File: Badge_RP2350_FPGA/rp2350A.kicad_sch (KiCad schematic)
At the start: 33 parts, among them J4 SM03B-SRSS-TB, SW1 SW_Push, SW2 SW_Push, U1 RP2350_60QFN, U3 W25Q128JVS, Y1 ABM8-272-T3

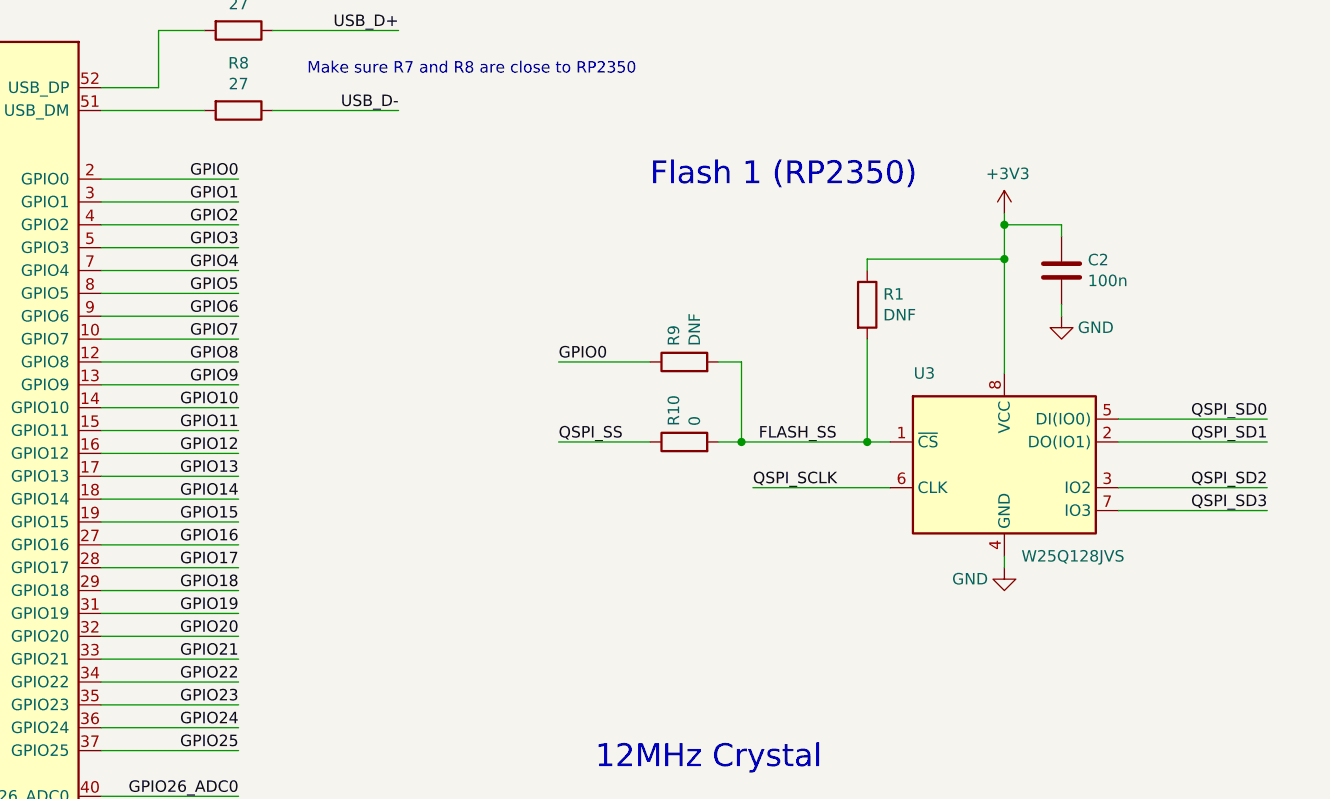
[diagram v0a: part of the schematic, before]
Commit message: add jtag connection
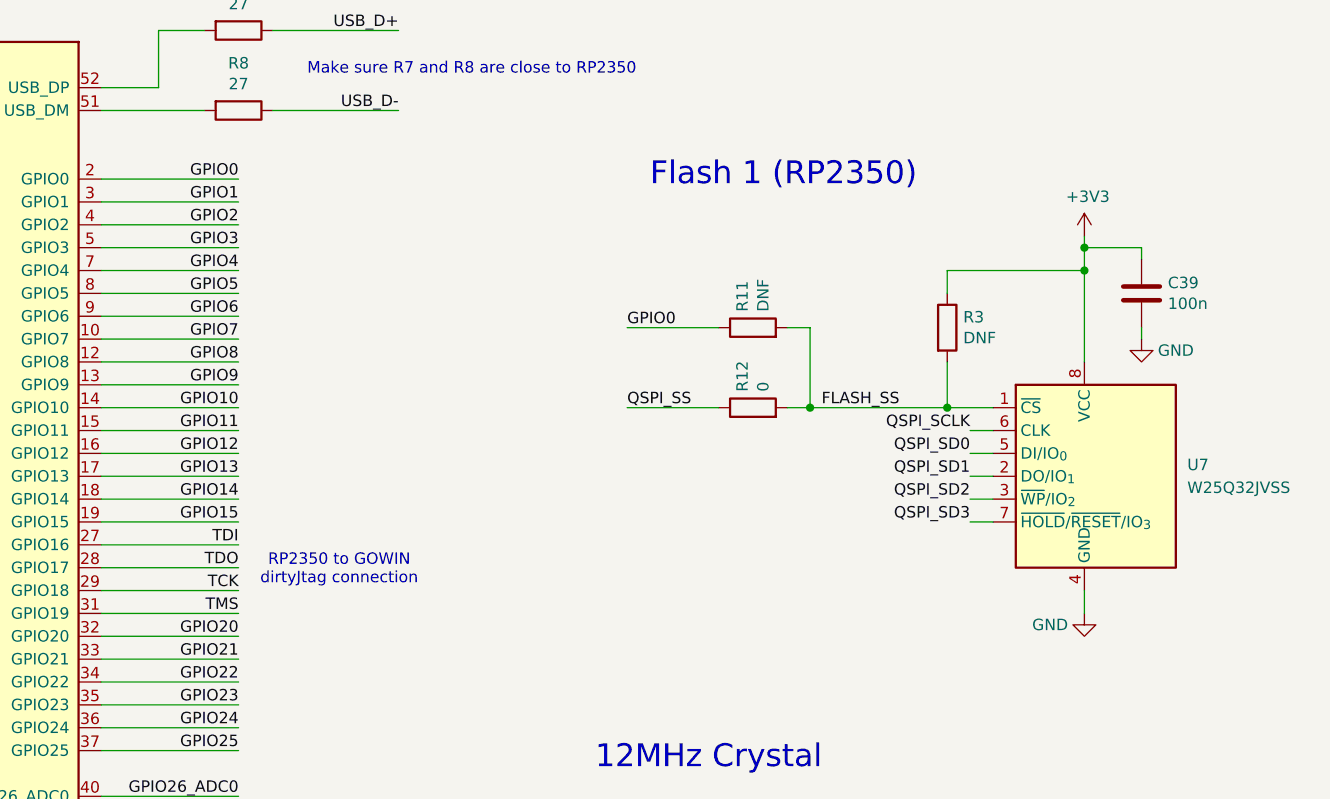
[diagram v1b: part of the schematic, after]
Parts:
- removed C2: 100n, Capacitor_SMD:C_0402_1005Metric, symbol Device:C
- removed R1, R9: DNF, Resistor_SMD:R_0402_1005Metric, symbol Device:R
- removed R10: 0, Resistor_SMD:R_0402_1005Metric, symbol Device:R
- removed U3: W25Q128JVS, Package_SO:SOIC-8_5.23x5.23mm_P1.27mm, symbol Memory_Flash:W25Q128JVS
- added C39: 100n, Capacitor_SMD:C_0402_1005Metric, symbol Device:C
- added R11, R3: DNF, Resistor_SMD:R_0402_1005Metric, symbol Device:R
- added R12: 0, Resistor_SMD:R_0402_1005Metric, symbol Device:R
- added U7: W25Q32JVSS, Package_SO:SOIC-8_5.3x5.3mm_P1.27mm, symbol Memory_Flash:W25Q32JVSS
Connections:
- net +3V3: now also C39.1, R3.1, U7.8 (VCC)
- net FLASH_SS: now also R11.2, R12.2, R3.2, U7.1 (~{CS})
- net GND: now also C39.2, U7.4 (GND)
- net GPIO0: now also R11.1
- net QSPI_SCLK: now also U7.6 (CLK)
- net QSPI_SD0: now also U7.5 (DI/IO_{0})
- net QSPI_SD1: now also U7.2 (DO/IO_{1})
- net QSPI_SD2: now also U7.3 (~{WP}/IO_{2})
- net QSPI_SD3: now also U7.7 (~{HOLD}/~{RESET}/IO_{3})
- net QSPI_SS: now also R12.1
- net GPIO16 renamed TDI
- net GPIO17 renamed TDO
- net GPIO18 renamed TCK
- net GPIO19 renamed TMS
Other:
- note added: "RP2350 to GOWIN dirtyJtag connection"

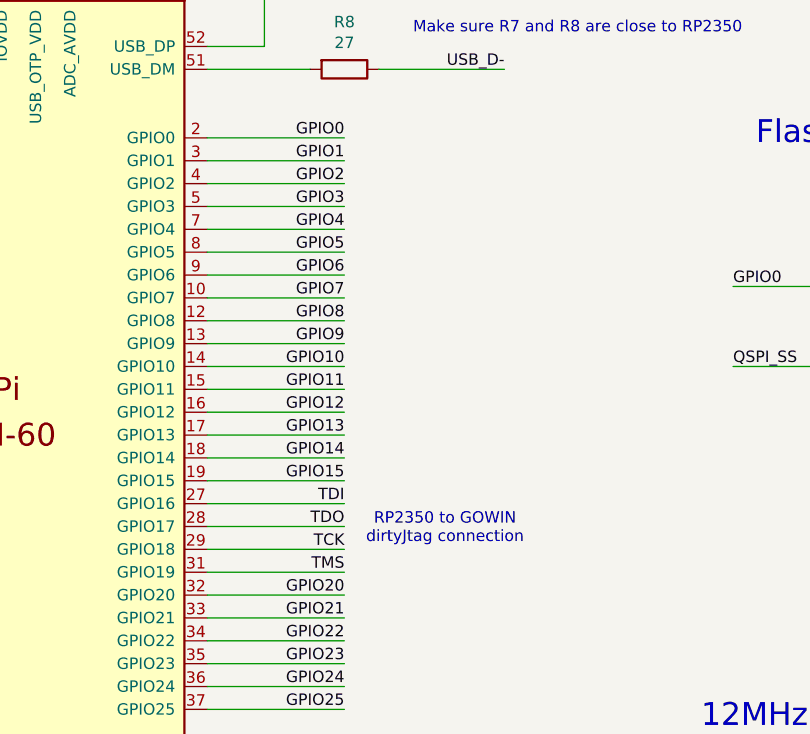
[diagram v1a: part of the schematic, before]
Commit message: add buttons by Arianna and make Flash 2 shared between 2 chips
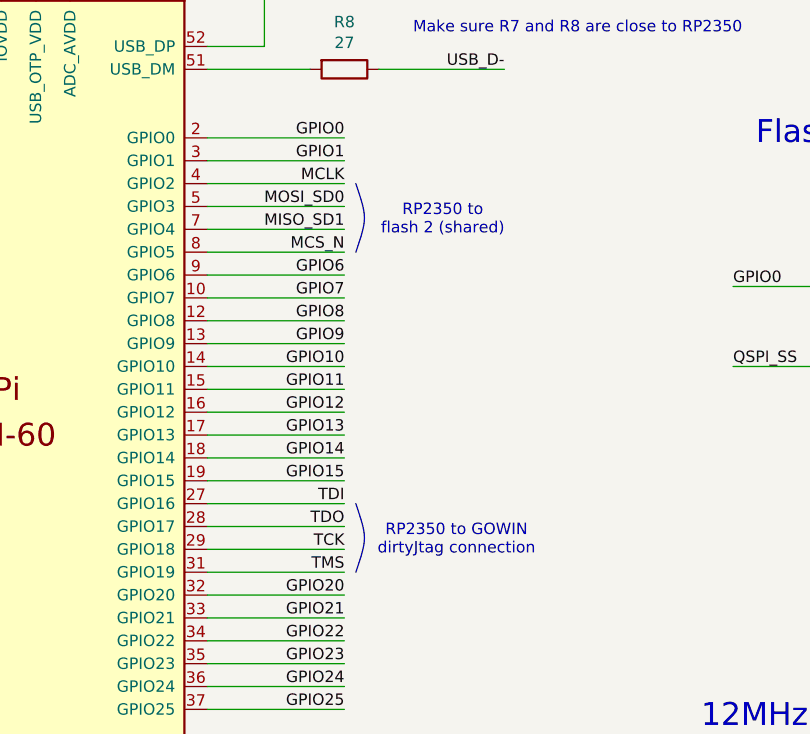
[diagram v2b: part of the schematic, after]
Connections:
- net GPIO2 renamed MCLK
- net GPIO3 renamed MOSI_SD0
- net GPIO4 renamed MISO_SD1
- net GPIO5 renamed MCS_N
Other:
- note added: "RP2350 to flash 2 (shared)"
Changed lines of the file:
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@@
 	(generator_version "10.0")
 	(paper "A4")
+	(bezier
+		(pts
+			(xy 156.21 76.2) (xy 157.48 80.01) (xy 157.48 80.01) (xy 156.21 83.82)
+		)
+		(stroke
+			(width 0)
+			(type default)
+		)
+		(fill
+			(type none)
+		)
+	)
+	(bezier
+		(pts
+			(xy 156.21 111.76) (xy 157.48 115.57) (xy 157.48 115.57) (xy 156.21 119.38)
+		)
+		(stroke
+			(width 0)
+			(type default)
+		)
+		(fill
+			(type none)
+		)
+	)
 	(circle
 		(center 43.18 65.405)
@@
 		)
 	)
+	(text "RP2350 to \nflash 2 (shared)"
+		(exclude_from_sim no)
+		(at 165.862 80.264 0)
+		(effects
+			(font
+				(size 1.27 1.27)
+			)
+		)
+	)
 	(text "JST Debug Connector"
 		(exclude_from_sim no)
@@
 	(text "RP2350 to GOWIN \ndirtyJtag connection"
 		(exclude_from_sim no)
-		(at 166.116 114.554 0)
+		(at 167.386 115.824 0)
 		(effects
 			(font
@@
 		)
 	)
-	(label "GPIO5"
-		(at 154.94 83.82 180)
-		(effects
-			(font
-				(size 1.27 1.27)
-			)
-			(justify right bottom)
-		)
-	)
 	(label "GPIO8"
 		(at 154.94 91.44 180)
@@
 		)
 	)
-	(label "GPIO2"
-		(at 154.94 76.2 180)
-		(effects
-			(font
-				(size 1.27 1.27)
-			)
-			(justify right bottom)
-		)
-	)
 	(label "GPIO27_ADC1"
 		(at 154.94 142.24 180)
@@
 		)
 	)
-	(label "GPIO4"
-		(at 154.94 81.28 180)
-		(effects
-			(font
-				(size 1.27 1.27)
-			)
-			(justify right bottom)
-		)
-	)
 	(label "QSPI_SD0"
 		(at 236.22 101.6 180)
@@
 		)
 	)
+	(label "MCS_N"
+		(at 154.94 83.82 180)
+		(effects
+			(font
+				(size 1.27 1.27)
+			)
+			(justify right bottom)
+		)
+	)
 	(label "QSPI_SCLK"
 		(at 236.22 99.06 180)
@@
 		)
 	)
+	(label "MCLK"
+		(at 154.94 76.2 180)
+		(effects
+			(font
+				(size 1.27 1.27)
+			)
+			(justify right bottom)
+		)
+	)
 	(label "USB_D-"
 		(at 172.72 63.5 180)
@@
 		)
 	)
-	(label "GPIO3"
-		(at 154.94 78.74 180)
-		(effects
-			(font
-				(size 1.27 1.27)
-			)
-			(justify right bottom)
-		)
-	)
 	(label "QSPI_SD3"
 		(at 236.22 109.22 180)
@@
 		)
 	)
+	(label "MOSI_SD0"
+		(at 154.94 78.74 180)
+		(effects
+			(font
+				(size 1.27 1.27)
+			)
+			(justify right bottom)
+		)
+	)
 	(label "GPIO12"
 		(at 154.94 101.6 180)
@@
 		)
 	)
+	(label "MISO_SD1"
+		(at 154.94 81.28 180)
+		(effects
+			(font
+				(size 1.27 1.27)
+			)
+			(justify right bottom)
+		)
+	)

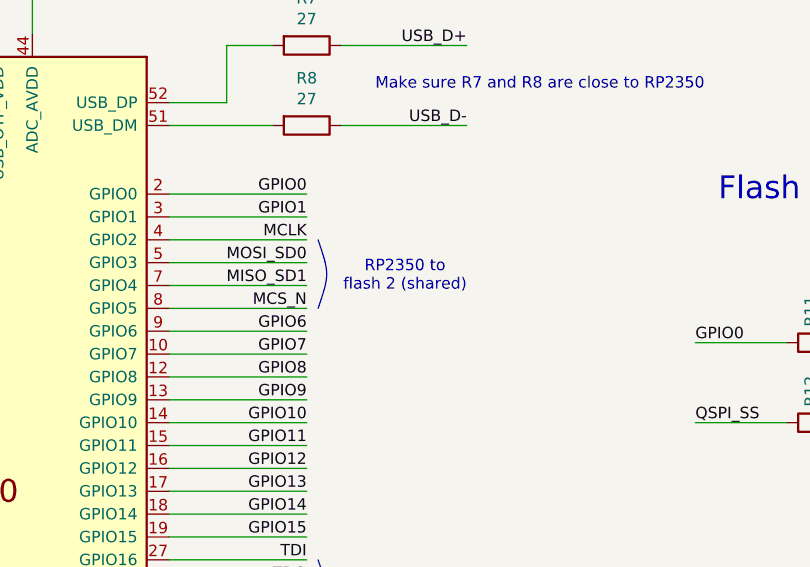
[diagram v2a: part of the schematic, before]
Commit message: delete Core directory - not the right repository
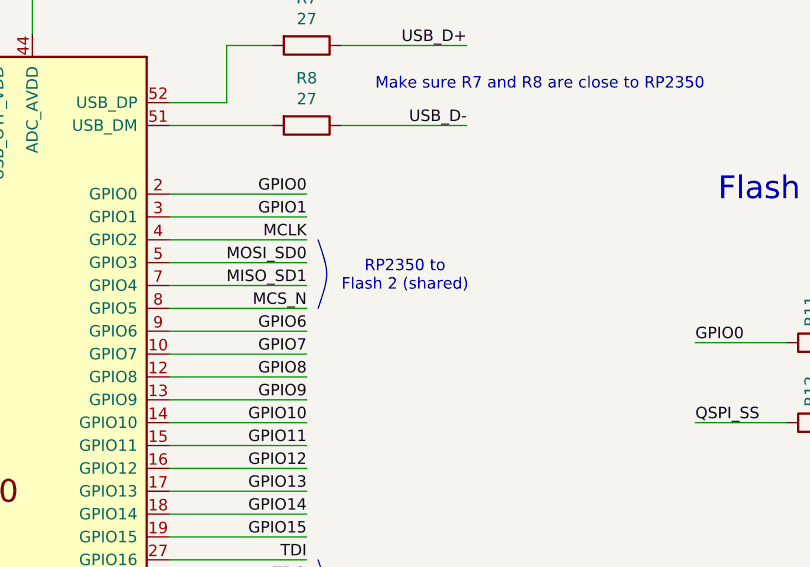
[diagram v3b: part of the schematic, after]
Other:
- note added: "RP2350 to Flash 2 (shared)"
- note removed: "RP2350 to flash 2 (shared)"
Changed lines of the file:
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@@
 		)
 	)
-	(text "RP2350 to \nflash 2 (shared)"
+	(text "RP2350 to \nFlash 2 (shared)"
 		(exclude_from_sim no)
 		(at 165.862 80.264 0)

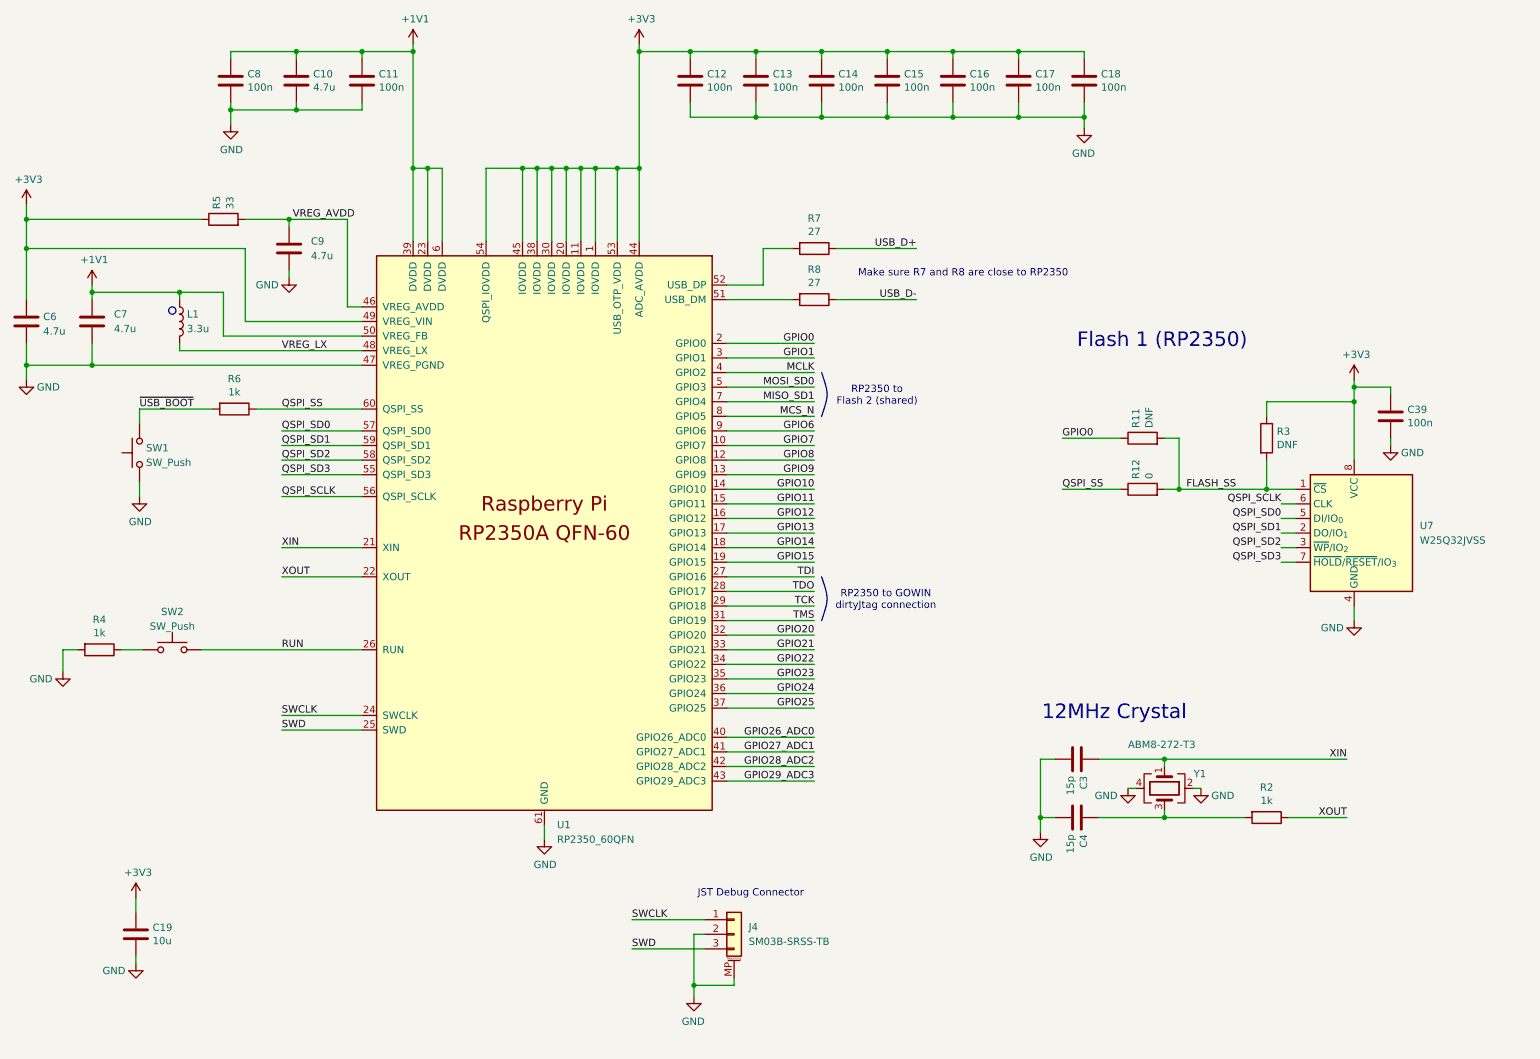
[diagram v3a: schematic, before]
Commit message: add type c port and uart connections
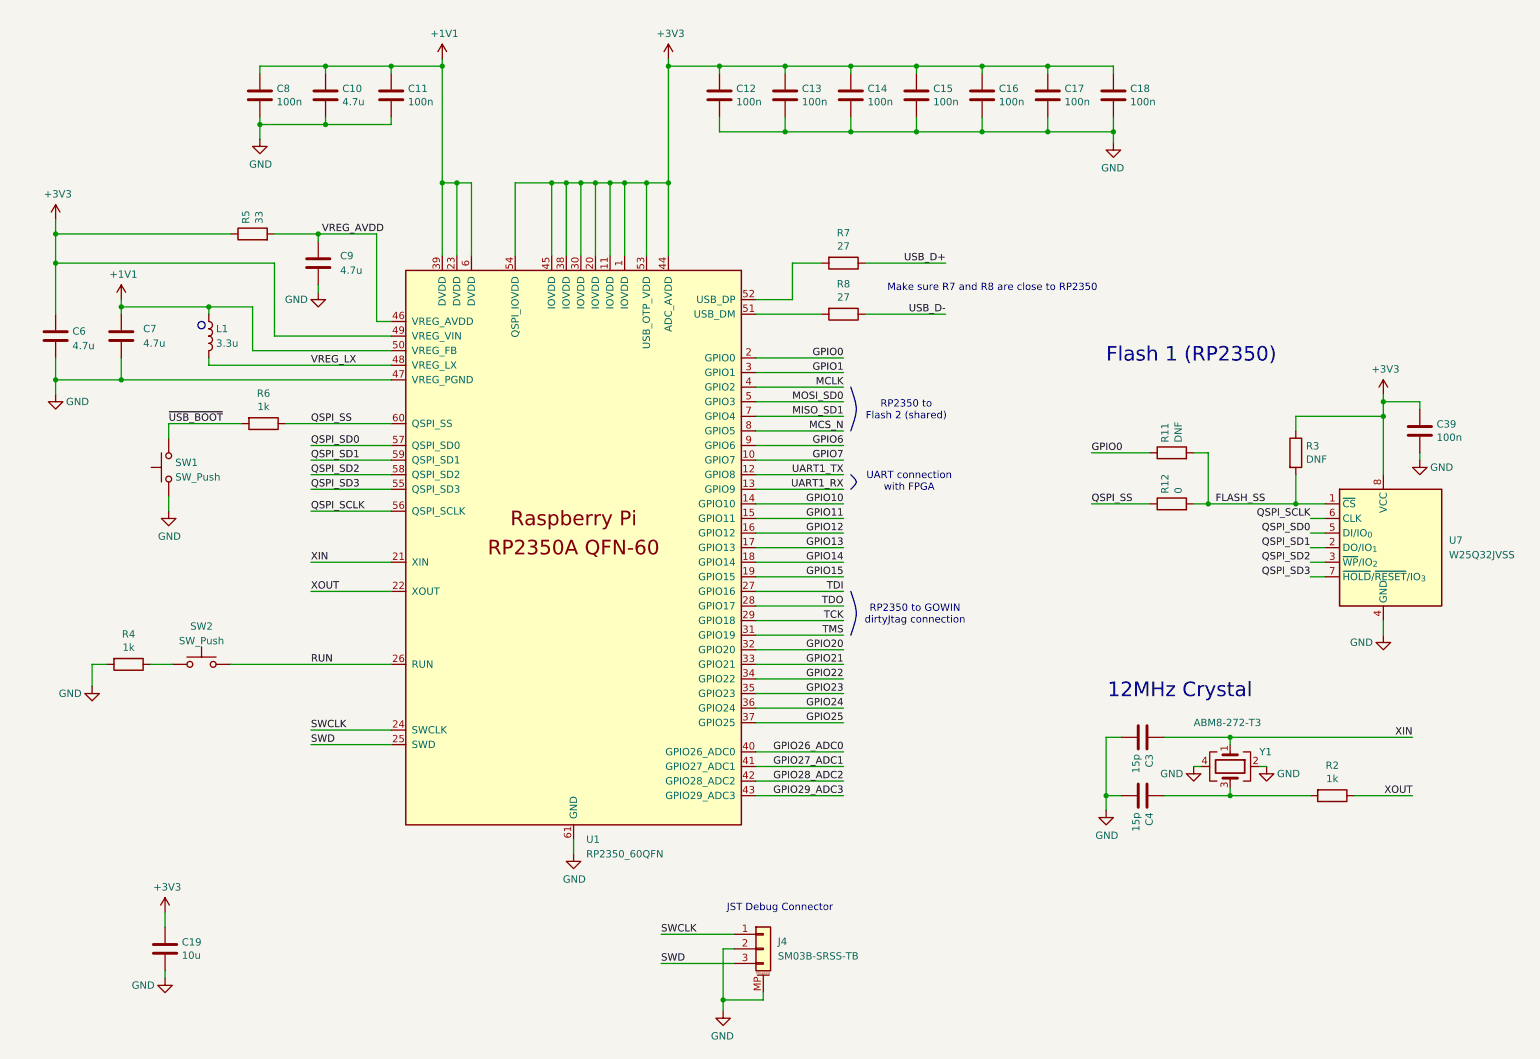
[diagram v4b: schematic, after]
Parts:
- C6, C7: footprint RP2350_60QFN_minimal:C_0402_1005Metric_small_pads -> Capacitor_SMD:C_0402_1005Metric
- L1: footprint RP2350_60QFN_minimal:L_pol_2016 -> semitovpartslibrary:L_pol_2016
- SW1, SW2: footprint Button_Switch_SMD:SW_Push_1P1T_NO_Vertical_Wuerth_434133025816 -> Button_Switch_SMD:SW_Push_1P1T_NO_CK_KSC6xxG
- U1: footprint RP2350_60QFN_minimal:RP2350-QFN-60-1EP_7x7_P0.4mm_EP3.4x3.4mm_ThermalVias -> semitovpartslibrary:RP2350-QFN-60-1EP_7x7_P0.4mm_EP3.4x3.4mm_ThermalVias
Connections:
- net GPIO8 renamed UART1_TX
- net GPIO9 renamed UART1_RX
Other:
- note added: "UART connection with FPGA"
- company: (none) -> SemiTO-V, RISC-V Student Team
- title: (none) -> RISC-V Summit Europe Badge
- moved on the sheet: C10, C11, C12, C13, C14, C15, C16, C17, C18, C19, C3, C39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
